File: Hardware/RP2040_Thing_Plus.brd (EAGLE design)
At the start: 22.9 x 58.4 mm, 132 parts, among them J1 CORTEX_JTAG_DEBUG_MINIMUM_PTH, J3 QWIIC_RIGHT_ANGLE, J5 USB Female Type C Connector, J6 MICRO-SD-SDIOPUSH-PUSH, Q1 2.5A/30V, U2 MAX17048, U3 MCP73831, U4 W25QXX128MBIT, U5 RP2040, U6 WS2812-2020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

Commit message: Run lib update on schematic. Compress schematic wires. Push production files.
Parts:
- J1: value CORTEX_JTAG_DEBUG_MINIMUM_PTH -> SWD
- J3: value QWIIC_RIGHT_ANGLE -> Qwiic
- J5: value USB Female Type C Connector -> USB C
- J6: value MICRO-SD-SDIOPUSH-PUSH -> microSD
- Q1: value 2.5A/30V -> 20V/4.2A/52mΩ/1.4W; device SparkFun-DiscreteSemi:SOT23-3@1 -> SparkFun-DiscreteSemi:SOT23-3
- R6: value 2.0KOHM-0402T-1/16W-5% -> 1k
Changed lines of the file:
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@@
 <layer number="19" name="Unrouted" color="6" fill="1" visible="yes" active="yes"/>
 <layer number="20" name="Dimension" color="24" fill="1" visible="yes" active="yes"/>
-<layer number="21" name="tPlace" color="16" fill="1" visible="no" active="yes"/>
-<layer number="22" name="bPlace" color="14" fill="1" visible="no" active="yes"/>
+<layer number="21" name="tPlace" color="16" fill="1" visible="yes" active="yes"/>
+<layer number="22" name="bPlace" color="14" fill="1" visible="yes" active="yes"/>
 <layer number="23" name="tOrigins" color="15" fill="1" visible="yes" active="yes"/>
-<layer number="24" name="bOrigins" color="15" fill="1" visible="no" active="yes"/>
+<layer number="24" name="bOrigins" color="15" fill="1" visible="yes" active="yes"/>
 <layer number="25" name="tNames" color="7" fill="1" visible="no" active="yes"/>
 <layer number="26" name="bNames" color="7" fill="1" visible="no" active="yes"/>
@@
 <layer number="43" name="vRestrict" color="2" fill="10" visible="no" active="yes"/>
 <layer number="44" name="Drills" color="7" fill="1" visible="no" active="yes"/>
-<layer number="45" name="Holes" color="7" fill="1" visible="no" active="yes"/>
+<layer number="45" name="Holes" color="7" fill="1" visible="yes" active="yes"/>
 <layer number="46" name="Milling" color="3" fill="1" visible="no" active="yes"/>
 <layer number="47" name="Measures" color="7" fill="1" visible="no" active="yes"/>
@@
 <layer number="49" name="Reference" color="7" fill="1" visible="no" active="yes"/>
 <layer number="50" name="dxf" color="7" fill="1" visible="no" active="yes"/>
-<layer number="51" name="tDocu" color="6" fill="1" visible="no" active="yes"/>
+<layer number="51" name="tDocu" color="6" fill="1" visible="yes" active="yes"/>
 <layer number="52" name="bDocu" color="7" fill="1" visible="no" active="yes"/>
 <layer number="91" name="Nets" color="2" fill="1" visible="no" active="no"/>
@@
 <layer number="95" name="Names" color="7" fill="1" visible="no" active="no"/>
 <layer number="96" name="Values" color="7" fill="1" visible="no" active="no"/>
-<layer number="2" name="gndvert" color="10" fill="7" visible="yes" active="yes"/>
-<layer number="15" name="pwrhorz" color="4" fill="7" visible="yes" active="yes"/>
+<layer number="2" name="gndvert" color="10" fill="7" visible="no" active="yes"/>
+<layer number="15" name="pwrhorz" color="4" fill="7" visible="no" active="yes"/>
 <layer number="3" name="Route3" color="4" fill="3" visible="no" active="no"/>
 <layer number="4" name="Route4" color="1" fill="4" visible="no" active="no"/>
@@
 <attribute name="VALUE" x="11.43" y="29.845" size="0.6096" layer="27" font="vector" ratio="20" align="top-center"/>
 </element>
-<element name="Q1" library="SparkFun-DiscreteSemi" package="SOT23-3@1" value="2.5A/30V" x="12.319" y="16.51" smashed="yes" rot="R90">
+<element name="Q1" library="SparkFun-DiscreteSemi" package="SOT23-3" value="20V/4.2A/52mΩ/1.4W" x="12.319" y="16.51" smashed="yes" rot="R90">
 <attribute name="NAME" x="10.541" y="15.6845" size="0.4064" layer="25" rot="R90"/>
-<attribute name="PROD_ID" value="TRANS-11308" x="50.419" y="-38.1" size="1.778" layer="27" font="vector" ratio="15" rot="R90" display="off"/>
-<attribute name="VALUE" x="12.5095" y="15.494" size="0.4064" layer="27" rot="R90"/>
+<attribute name="PROD_ID" value="TRAN-14388" x="50.419" y="-38.1" size="1.778" layer="27" font="vector" ratio="15" rot="R90" display="off"/>
+<attribute name="VALUE" value="20V/4.2A/52mΩ/1.4W" x="12.5095" y="15.494" size="0.4064" layer="27" rot="R90"/>
 </element>
 <element name="D4" library="SparkFun-LED" package="LED-0603" value="BLUE" x="11.43" y="33.02" smashed="yes" rot="R180">
@@
 <element name="FD1" library="SparkFun-Aesthetics" package="FIDUCIAL-MICRO" value="FIDUCIALUFIDUCIAL" x="1.27" y="5.08" smashed="yes"/>
 <element name="FD2" library="SparkFun-Aesthetics" package="FIDUCIAL-MICRO" value="FIDUCIALUFIDUCIAL" x="17.78" y="57.15" smashed="yes"/>
-<element name="J3" library="SparkFun-Connectors" package="JST04_1MM_RA" value="QWIIC_RIGHT_ANGLE" x="5.08" y="9.398" smashed="yes" rot="R270">
+<element name="J3" library="SparkFun-Connectors" package="JST04_1MM_RA" value="Qwiic" x="5.08" y="9.398" smashed="yes" rot="R270">
 <attribute name="NAME" x="2.921" y="10.795" size="0.6096" layer="25" font="vector" ratio="20" rot="R270"/>
 <attribute name="PROD_ID" value="CONN-13694" x="5.08" y="9.398" size="1.778" layer="27" font="vector" ratio="15" rot="R270" display="off"/>
@@
 <attribute name="VALUE" x="3.789" y="44.442" size="0.6096" layer="27" font="vector" ratio="12" rot="R270" align="top-center"/>
 </element>
-<element name="J5" library="SparkFun-Connectors" package="USB-C-16P-4LAYER-ISOLATED" value="USB Female Type C Connector" x="11.43" y="6.35" smashed="yes">
+<element name="J5" library="SparkFun-Connectors" package="USB-C-16P-4LAYER-ISOLATED" value="USB C" x="11.43" y="6.35" smashed="yes">
 <attribute name="NAME" x="11.43" y="3.81" size="0.762" layer="25" align="center"/>
 <attribute name="PROD_ID" value="CONN-14122" x="11.43" y="6.35" size="1.778" layer="27" font="vector" ratio="15" display="off"/>
@@
 <attribute name="VALUE" x="18.796" y="12.954" size="0.6096" layer="27" font="vector" ratio="20" rot="R180" align="top-center"/>
 </element>
-<element name="J6" library="SparkFun-Connectors" package="MICRO-SD-SOCKET" value="MICRO-SD-SDIOPUSH-PUSH" x="5.969" y="38.354" smashed="yes" rot="MR0">
+<element name="J6" library="SparkFun-Connectors" package="MICRO-SD-SOCKET" value="microSD" x="5.969" y="38.354" smashed="yes" rot="MR0">
 <attribute name="NAME" x="14.859" y="44.704" size="0.6096" layer="26" font="vector" ratio="20" rot="MR0"/>
 <attribute name="PROD_ID" value="CONN-07820" x="5.969" y="38.354" size="1.778" layer="28" font="vector" ratio="15" rot="MR0" display="off"/>
@@
 <attribute name="VALUE" x="8.455" y="33.528" size="0.6096" layer="27" font="vector" ratio="20" rot="R270" align="top-center"/>
 </element>
-<element name="J1" library="SparkFun-Connectors" package="2X5-PTH-1.27MM" value="CORTEX_JTAG_DEBUG_MINIMUM_PTH" x="6.35" y="34.29" smashed="yes" rot="R270">
+<element name="J1" library="SparkFun-Connectors" package="2X5-PTH-1.27MM" value="SWD" x="6.35" y="34.29" smashed="yes" rot="R270">
 <attribute name="NAME" x="8.2804" y="35.8648" size="0.6096" layer="25" font="vector" ratio="20" rot="R270"/>
 <attribute name="VALUE" x="3.8862" y="36.1188" size="0.6096" layer="27" font="vector" ratio="20" rot="R270"/>
@@
 <attribute name="VALUE" x="14.297" y="26.162" size="0.6096" layer="27" font="vector" ratio="20" rot="R270" align="top-center"/>
 </element>
-<element name="R6" library="SparkFun-Resistors" package="0402-TIGHT" value="2.0KOHM-0402T-1/16W-5%" x="9.144" y="25.654" smashed="yes" rot="R270">
+<element name="R6" library="SparkFun-Resistors" package="0402-TIGHT" value="1k" x="9.144" y="25.654" smashed="yes" rot="R270">
 <attribute name="NAME" x="9.706" y="25.654" size="0.6096" layer="25" font="vector" ratio="20" rot="R270" align="bottom-center"/>
-<attribute name="VALUE" x="8.582" y="25.654" size="0.6096" layer="27" font="vector" ratio="20" rot="R270" align="top-center"/>
+<attribute name="PROD_ID" value="RES-14342" x="9.144" y="25.654" size="1.778" layer="27" rot="R270" display="off"/>
+<attribute name="VALUE" value="1k" x="8.582" y="25.654" size="0.6096" layer="27" font="vector" ratio="20" rot="R270" align="top-center"/>
 </element>
 <element name="U$1" library="output" package="#_16#0" value="" x="1.651" y="31.75" smashed="yes"/>
@@
 <contactref element="JP1" pad="3"/>
 <contactref element="R10" pad="2"/>
-<wire x1="8.763" y1="8.255" x2="8.5344" y2="8.4836" width="0.127" layer="16"/>
 <wire x1="8.5344" y1="8.4836" x2="8.255" y2="8.4836" width="0.127" layer="16"/>
 <wire x1="8.255" y1="8.4836" x2="9.7964" y2="8.4836" width="0.127" layer="16"/>

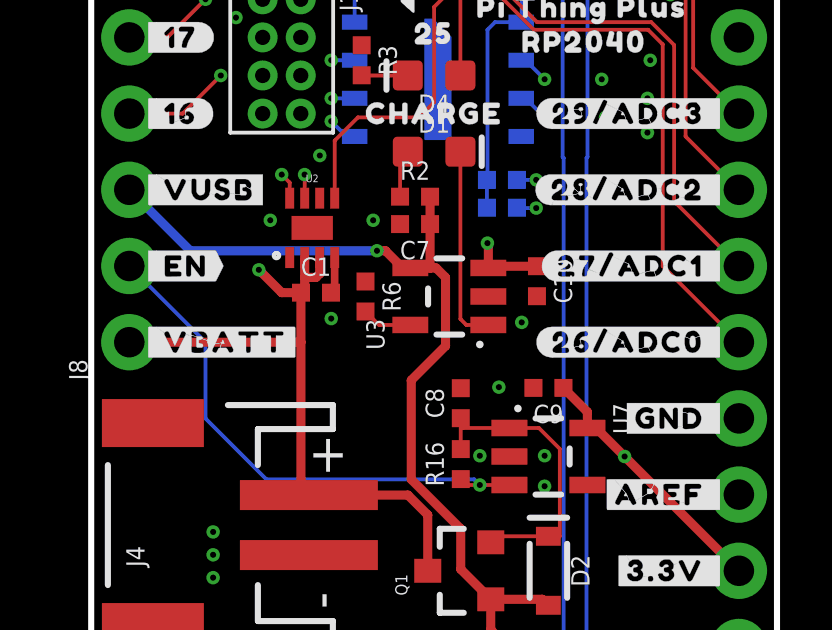
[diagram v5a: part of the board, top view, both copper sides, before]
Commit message: Change res on charger to 2k
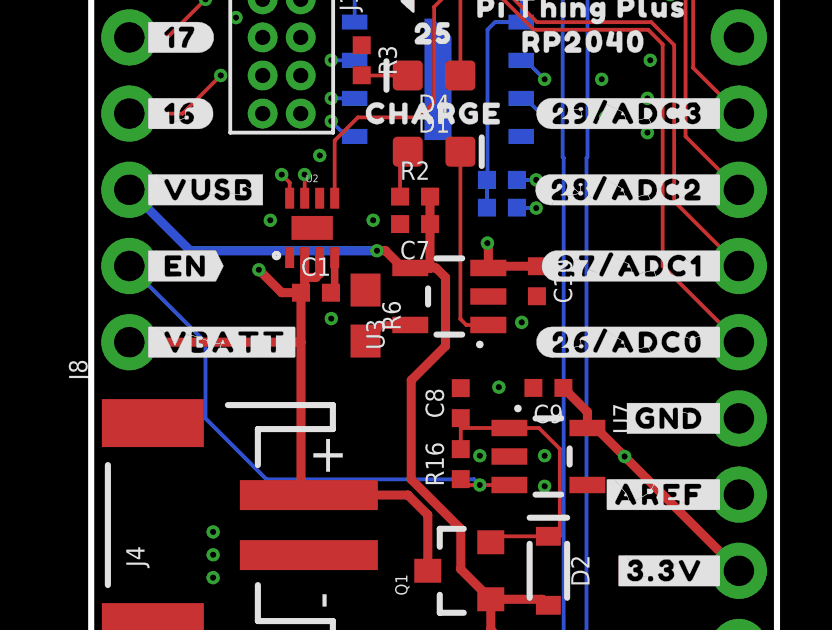
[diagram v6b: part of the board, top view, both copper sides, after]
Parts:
- R6: value 1k -> 2.0k; device SparkFun-Resistors:0402-TIGHT -> SparkFun-Resistors:0603
- moved R6 0.64 mm to (9.14, 25.0)
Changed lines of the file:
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@@
 <attribute name="VALUE" x="14.297" y="26.162" size="0.6096" layer="27" font="vector" ratio="20" rot="R270" align="top-center"/>
 </element>
-<element name="R6" library="SparkFun-Resistors" package="0402-TIGHT" value="1k" x="9.144" y="25.654" smashed="yes" rot="R270">
-<attribute name="NAME" x="9.706" y="25.654" size="0.6096" layer="25" font="vector" ratio="20" rot="R270" align="bottom-center"/>
-<attribute name="PROD_ID" value="RES-14342" x="9.144" y="25.654" size="1.778" layer="27" rot="R270" display="off"/>
-<attribute name="VALUE" value="1k" x="8.582" y="25.654" size="0.6096" layer="27" font="vector" ratio="20" rot="R270" align="top-center"/>
+<element name="R6" library="SparkFun-Resistors" package="0603" value="2.0k" x="9.144" y="25.019" smashed="yes" rot="R270">
+<attribute name="NAME" x="9.706" y="25.019" size="0.6096" layer="25" font="vector" ratio="20" rot="R270" align="bottom-center"/>
+<attribute name="PROD_ID" value="RES-08296" x="9.144" y="25.019" size="1.778" layer="27" rot="R270" display="off"/>
+<attribute name="VALUE" value="2.0k" x="8.582" y="25.019" size="0.6096" layer="27" font="vector" ratio="20" rot="R270" align="top-center"/>
 </element>
 <element name="U$1" library="output" package="#_16#0" value="" x="1.651" y="31.75" smashed="yes"/>
@@
 <contactref element="U3" pad="5"/>
 <contactref element="R6" pad="2"/>
-<wire x1="9.144" y1="25.154" x2="9.594" y2="24.704" width="0.127" layer="1"/>
-<wire x1="9.594" y1="24.704" x2="10.6379" y2="24.704" width="0.127" layer="1"/>
+<wire x1="10.6379" y1="24.704" x2="9.679" y2="24.704" width="0.254" layer="1"/>
+<wire x1="9.679" y1="24.704" x2="9.144" y2="24.169" width="0.254" layer="1"/>
 </signal>
 <signal name="V_BATT">

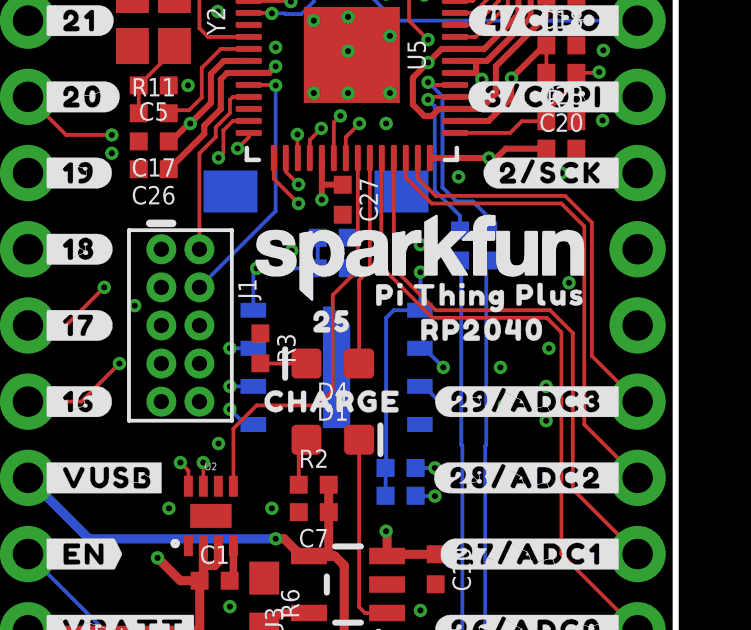
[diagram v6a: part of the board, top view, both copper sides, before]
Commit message: Correct product name silk
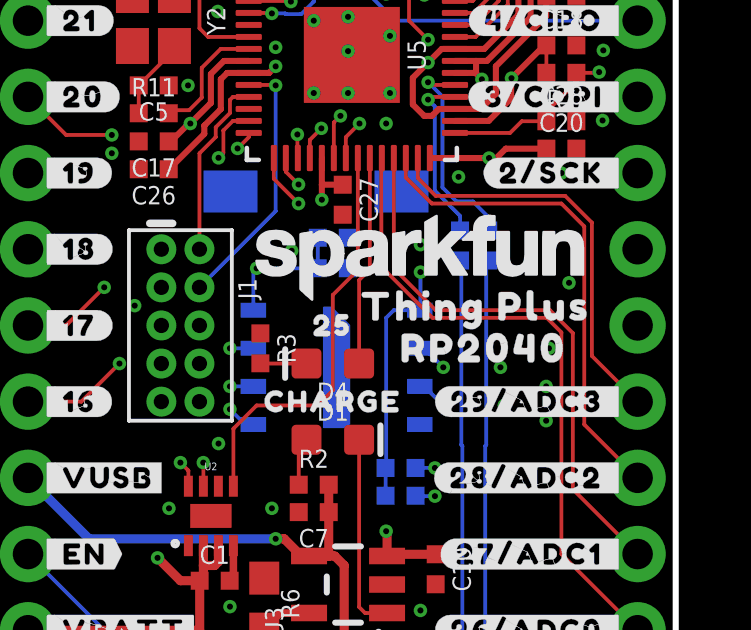
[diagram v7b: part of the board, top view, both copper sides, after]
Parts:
- removed U$29: (no value), output:PI_THING_PLUS0
- removed U$30: (no value), output:RP20400
- added U$46: (no value), output:RP2040_1
- added U$47: (no value), output:THING_PLUS_0
- U$43: device output:PI_THING_PLUS_0 -> output:RP20401
- U$44: device output:RP2040_0 -> output:THING_PLUS0
- moved U$43 23.4 mm to (6.22, 14.2), flipped to the bottom
- moved U$44 20.4 mm to (6.48, 16.4), flipped to the bottom
- moved U$54 0.13 mm to (11.4, 34.3)

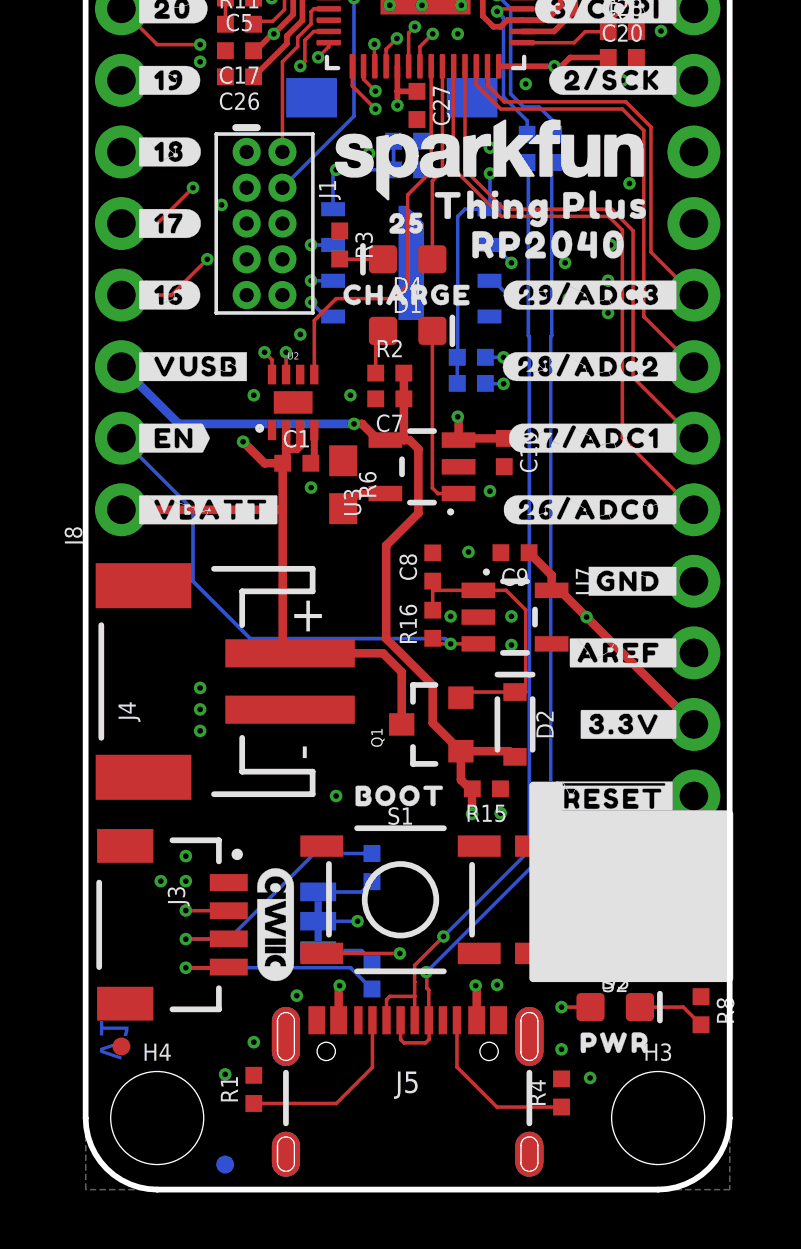
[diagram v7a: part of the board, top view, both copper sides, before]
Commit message: Panel with 2k charge resistor
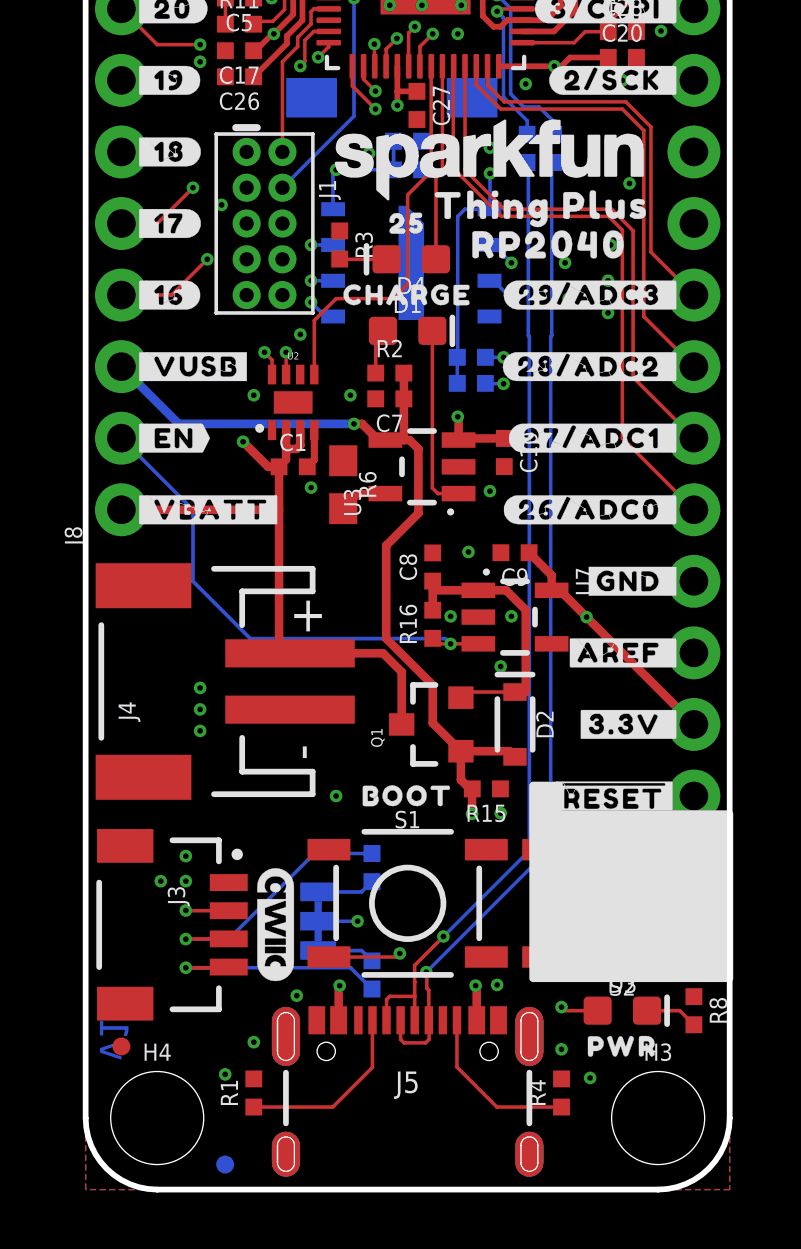
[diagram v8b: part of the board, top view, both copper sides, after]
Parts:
- removed LOGO1: FOUR_LAYER_WARNING, SparkFun-Aesthetics:FOUR_LAYER_WARNING
- moved D3 0.28 mm to (19.1, 6.35)
- moved S2 0.28 mm to (19.1, 10.2)
- moved U$16 0.28 mm to (19.1, 5.08)
- moved S1 0.28 mm to (11.4, 10.2)
- moved R8 0.25 mm to (21.6, 6.35)
- moved U$56 0.25 mm to (11.4, 14.0)
- moved C1 0.18 mm to (7.37, 25.7)
- moved D4 0.13 mm to (11.6, 33.0)
- moved R1 0.13 mm to (5.97, 3.43)
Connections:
- net SDIO_DAT1/AUD_IN renamed SDIO_DAT1
- net SDIO_DAT2/AUD_OUT renamed SDIO_DAT2
- removed net N$13: U5.7
- removed net N$24: U5.16
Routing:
- net N$7: track 2.43 -> 1.87 mm
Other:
- board text added: "1.6mm FR4"
- board text added: "Four Layer"
